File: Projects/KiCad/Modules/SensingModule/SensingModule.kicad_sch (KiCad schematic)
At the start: 40 parts, among them J1 Conn_01x02, J2 Conn_01x08, J3 Conn_01x02_Pin, J4 Micro_SD_Card_Det_Hirose_DM3AT, SW1 SW_DIP_x02, U1 MCP2562-E-P, U4 TLP222A, U5 NUCLEO-F303K8, U6 MB85RS2MT, U7 MB85RS2MT

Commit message: チップ積層セラミックコンデンサをSMD1608に変更
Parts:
- C1, C2: footprint Capacitor_SMD:C_0805_2012Metric_Pad1.18x1.45mm_HandSolder -> Capacitor_SMD:C_0603_1608Metric_Pad1.08x0.95mm_HandSolder
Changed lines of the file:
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@@
       (effects (font (size 1.27 1.27)) (justify left))
     )
-    (property "Footprint" "Capacitor_SMD:C_0805_2012Metric_Pad1.18x1.45mm_HandSolder" (at 93.6752 35.56 0)
+    (property "Footprint" "Capacitor_SMD:C_0603_1608Metric_Pad1.08x0.95mm_HandSolder" (at 93.6752 35.56 0)
       (effects (font (size 1.27 1.27)) hide)
     )
@@
       (effects (font (size 1.27 1.27)) (justify left))
     )
-    (property "Footprint" "Capacitor_SMD:C_0805_2012Metric_Pad1.18x1.45mm_HandSolder" (at 84.7852 35.56 0)
-      (effects (font (size 1.27 1.27)) hide)
-    )
+    (property "Footprint" "Capacitor_SMD:C_0603_1608Metric_Pad1.08x0.95mm_HandSolder" (at 84.7852 35.56 0)
+      (effects (font (size 1.27 1.27)) hide)
+    )

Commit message: 抵抗の在庫に合わせてサイズを変更
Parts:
- R1, R3, R4, R5, R9: footprint Resistor_SMD:R_0603_1608Metric_Pad0.98x0.95mm_HandSolder -> Resistor_SMD:R_0805_2012Metric_Pad1.20x1.40mm_HandSolder
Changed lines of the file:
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@@
       (effects (font (size 1.27 1.27)) (justify left))
     )
-    (property "Footprint" "Resistor_SMD:R_0603_1608Metric_Pad0.98x0.95mm_HandSolder" (at 230.632 48.26 90)
+    (property "Footprint" "Resistor_SMD:R_0805_2012Metric_Pad1.20x1.40mm_HandSolder" (at 230.632 48.26 90)
       (effects (font (size 1.27 1.27)) hide)
     )
@@
       (effects (font (size 1.27 1.27)) (justify left))
     )
-    (property "Footprint" "Resistor_SMD:R_0603_1608Metric_Pad0.98x0.95mm_HandSolder" (at 35.052 170.18 90)
+    (property "Footprint" "Resistor_SMD:R_0805_2012Metric_Pad1.20x1.40mm_HandSolder" (at 35.052 170.18 90)
       (effects (font (size 1.27 1.27)) hide)
     )
@@
       (effects (font (size 1.27 1.27)) (justify left))
     )
-    (property "Footprint" "Resistor_SMD:R_0603_1608Metric_Pad0.98x0.95mm_HandSolder" (at 35.052 123.19 90)
+    (property "Footprint" "Resistor_SMD:R_0805_2012Metric_Pad1.20x1.40mm_HandSolder" (at 35.052 123.19 90)
       (effects (font (size 1.27 1.27)) hide)
     )
@@
       (effects (font (size 1.27 1.27)) (justify left))
     )
-    (property "Footprint" "Resistor_SMD:R_0603_1608Metric_Pad0.98x0.95mm_HandSolder" (at 40.132 123.19 90)
+    (property "Footprint" "Resistor_SMD:R_0805_2012Metric_Pad1.20x1.40mm_HandSolder" (at 40.132 123.19 90)
       (effects (font (size 1.27 1.27)) hide)
     )
@@
       (effects (font (size 1.27 1.27)) (justify left))
     )
-    (property "Footprint" "Resistor_SMD:R_0603_1608Metric_Pad0.98x0.95mm_HandSolder" (at 220.472 48.26 90)
-      (effects (font (size 1.27 1.27)) hide)
-    )
+    (property "Footprint" "Resistor_SMD:R_0805_2012Metric_Pad1.20x1.40mm_HandSolder" (at 220.472 48.26 90)
+      (effects (font (size 1.27 1.27)) hide)
+    )

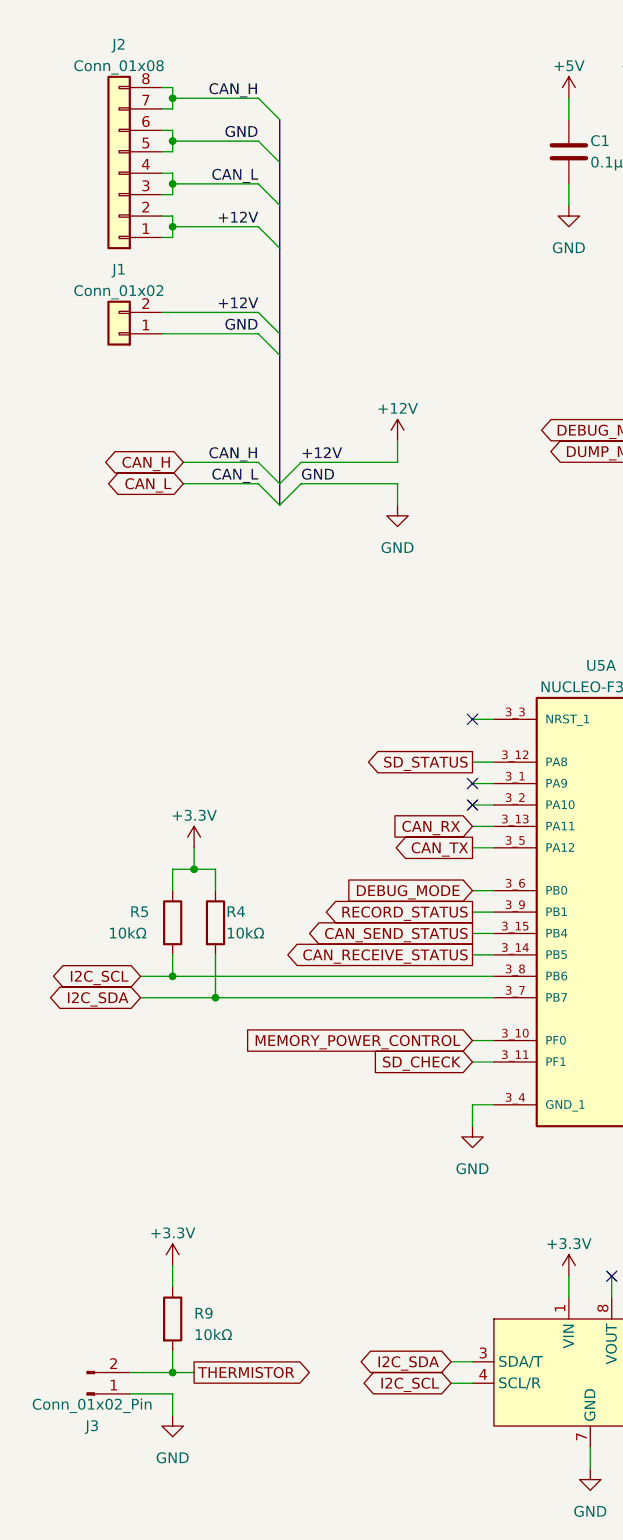
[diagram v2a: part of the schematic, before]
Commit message: コネクタ位置を揃えた
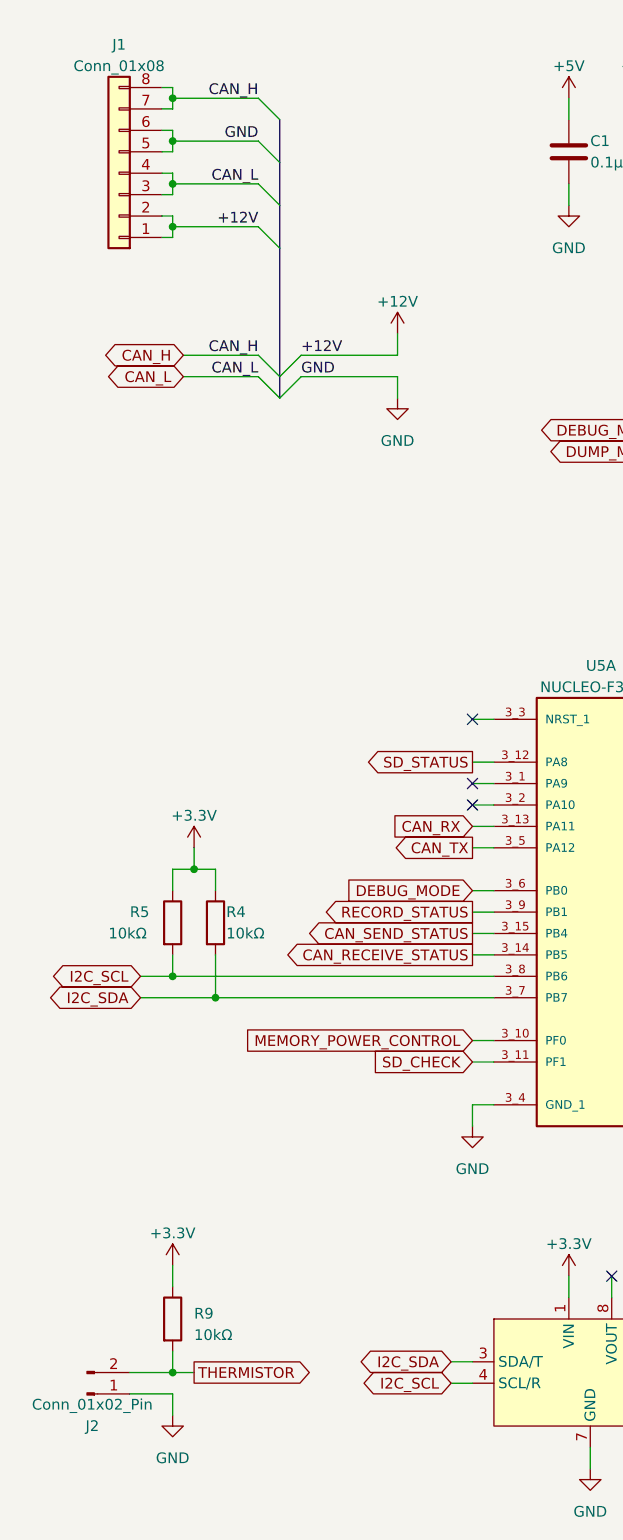
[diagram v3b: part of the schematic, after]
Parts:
- removed J1: Conn_01x02, Hirose_Connector:Hirose_DF1B, symbol Connector_Generic:Conn_01x02
- J1: renamed from J2; footprint Connector_Hirose:Hirose_DF11-8DP-2DSA_2x04_P2.00mm_Vertical -> Hirose_Connector:Hirose_DF11B-8DP-2DS
- renumbered J3 to J2
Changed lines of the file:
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@@
     (stroke (width 0) (type default))
   )
-  (bus_entry (at 49.53 71.12) (size 2.54 -2.54)
-    (stroke (width 0) (type default))
-  )
-  (bus_entry (at 46.99 53.34) (size 2.54 2.54)
-    (stroke (width 0) (type default))
-  )
-  (bus_entry (at 49.53 73.66) (size 2.54 -2.54)
+  (bus_entry (at 49.53 58.42) (size 2.54 -2.54)
+    (stroke (width 0) (type default))
+  )
+  (bus_entry (at 49.53 60.96) (size 2.54 -2.54)
     (stroke (width 0) (type default))
   )
@@
     (stroke (width 0) (type default))
   )
-  (bus_entry (at 46.99 50.8) (size 2.54 2.54)
-    (stroke (width 0) (type default))
-  )
   (bus_entry (at 46.99 30.48) (size 2.54 2.54)
     (stroke (width 0) (type default))
   )
-  (bus_entry (at 49.53 73.66) (size -2.54 -2.54)
-    (stroke (width 0) (type default))
-  )
-  (bus_entry (at 49.53 71.12) (size -2.54 -2.54)
+  (bus_entry (at 49.53 60.96) (size -2.54 -2.54)
+    (stroke (width 0) (type default))
+  )
+  (bus_entry (at 49.53 58.42) (size -2.54 -2.54)
     (stroke (width 0) (type default))
   )
@@
     (stroke (width 0) (type default))
   )
-  (wire (pts (xy 46.99 68.58) (xy 38.1 68.58))
-    (stroke (width 0) (type default))
-  )
-  (wire (pts (xy 35.56 50.8) (xy 46.99 50.8))
+  (wire (pts (xy 46.99 55.88) (xy 38.1 55.88))
     (stroke (width 0) (type default))
   )
@@
     (stroke (width 0) (type default))
   )
-  (bus (pts (xy 49.53 53.34) (xy 49.53 55.88))
-    (stroke (width 0) (type default))
-  )
   (wire (pts (xy 41.91 132.08) (xy 74.93 132.08))
     (stroke (width 0) (type default))
@@
     (stroke (width 0) (type default))
   )
-  (bus (pts (xy 49.53 71.12) (xy 49.53 73.66))
+  (bus (pts (xy 49.53 58.42) (xy 49.53 60.96))
     (stroke (width 0) (type default))
   )
@@
     (stroke (width 0) (type default))
   )
-  (wire (pts (xy 63.5 68.58) (xy 52.07 68.58))
+  (wire (pts (xy 63.5 55.88) (xy 52.07 55.88))
     (stroke (width 0) (type default))
   )
@@
     (stroke (width 0) (type default))
   )
-  (wire (pts (xy 63.5 66.04) (xy 63.5 68.58))
+  (wire (pts (xy 63.5 53.34) (xy 63.5 55.88))
     (stroke (width 0) (type default))
   )
@@
     (stroke (width 0) (type default))
   )
-  (bus (pts (xy 49.53 55.88) (xy 49.53 71.12))
+  (bus (pts (xy 49.53 43.18) (xy 49.53 58.42))
     (stroke (width 0) (type default))
   )
@@
     (stroke (width 0) (type default))
   )
-  (wire (pts (xy 46.99 71.12) (xy 38.1 71.12))
+  (wire (pts (xy 46.99 58.42) (xy 38.1 58.42))
     (stroke (width 0) (type default))
   )
@@
     (stroke (width 0) (type default))
   )
-  (bus (pts (xy 49.53 43.18) (xy 49.53 53.34))
-    (stroke (width 0) (type default))
-  )
   (wire (pts (xy 167.64 137.16) (xy 170.18 137.16))
     (stroke (width 0) (type default))
@@
     (stroke (width 0) (type default))
   )
-  (wire (pts (xy 63.5 71.12) (xy 52.07 71.12))
+  (wire (pts (xy 63.5 58.42) (xy 52.07 58.42))
     (stroke (width 0) (type default))
   )
@@
     (stroke (width 0) (type default))
   )
-  (wire (pts (xy 35.56 53.34) (xy 46.99 53.34))
-    (stroke (width 0) (type default))
-  )
   (wire (pts (xy 151.13 40.64) (xy 153.67 40.64))
     (stroke (width 0) (type default))
@@
     (stroke (width 0) (type default))
   )
-  (wire (pts (xy 63.5 73.66) (xy 63.5 71.12))
-    (stroke (width 0) (type default))
-  )
-  (label "+12V" (at 46.99 50.8 180) (fields_autoplaced)
-    (effects (font (size 1.27 1.27)) (justify right bottom))
+  (wire (pts (xy 63.5 60.96) (xy 63.5 58.42))
+    (stroke (width 0) (type default))
   )
   (label "CAN_L" (at 46.99 35.56 180) (fields_autoplaced)
@@
     (effects (font (size 1.27 1.27)) (justify right bottom))
   )
-  (label "GND" (at 46.99 53.34 180) (fields_autoplaced)
-    (effects (font (size 1.27 1.27)) (justify right bottom))
-  )
   (label "+12V" (at 46.99 40.64 180) (fields_autoplaced)
     (effects (font (size 1.27 1.27)) (justify right bottom))
   )
-  (label "GND" (at 52.07 71.12 0) (fields_autoplaced)
+  (label "GND" (at 52.07 58.42 0) (fields_autoplaced)
     (effects (font (size 1.27 1.27)) (justify left bottom))
   )
-  (label "CAN_H" (at 46.99 68.58 180) (fields_autoplaced)
+  (label "CAN_H" (at 46.99 55.88 180) (fields_autoplaced)
     (effects (font (size 1.27 1.27)) (justify right bottom))
   )
-  (label "+12V" (at 52.07 68.58 0) (fields_autoplaced)
+  (label "+12V" (at 52.07 55.88 0) (fields_autoplaced)
     (effects (font (size 1.27 1.27)) (justify left bottom))
   )
@@
     (effects (font (size 1.27 1.27)) (justify right bottom))
   )
-  (label "CAN_L" (at 46.99 71.12 180) (fields_autoplaced)
+  (label "CAN_L" (at 46.99 58.42 180) (fields_autoplaced)
     (effects (font (size 1.27 1.27)) (justify right bottom))
   )
@@
     )
   )
-  (global_label "CAN_L" (shape bidirectional) (at 38.1 71.12 180) (fields_autoplaced)
+  (global_label "CAN_L" (shape bidirectional) (at 38.1 58.42 180) (fields_autoplaced)
     (effects (font (size 1.27 1.27)) (justify right))
-    (property "Intersheetrefs" "${INTERSHEET_REFS}" (at 28.3981 71.12 0)
+    (property "Intersheetrefs" "${INTERSHEET_REFS}" (at 28.3981 58.42 0)
       (effects (font (size 1.27 1.27)) (justify right) hide)
     )
@@
     )
   )
-  (global_label "CAN_H" (shape bidirectional) (at 38.1 68.58 180) (fields_autoplaced)
+  (global_label "CAN_H" (shape bidirectional) (at 38.1 55.88 180) (fields_autoplaced)
     (effects (font (size 1.27 1.27)) (justify right))
-    (property "Intersheetrefs" "${INTERSHEET_REFS}" (at 28.0957 68.58 0)
+    (property "Intersheetrefs" "${INTERSHEET_REFS}" (at 28.0957 55.88 0)
       (effects (font (size 1.27 1.27)) (justify right) hide)
     )
@@
   (symbol (lib_id "Connector:Conn_01x02_Pin") (at 26.67 179.07 0) (mirror x) (unit 1)
     (in_bom yes) (on_board yes) (dnp no)
-    (property "Reference" "J3" (at 27.305 182.88 0)
+    (property "Reference" "J2" (at 27.305 182.88 0)
       (effects (font (size 1.27 1.27)))
     )
@@
       (project "SensingModule"
         (path "/ea1ed597-7cd3-4340-902e-bdce8f2d7a62"
-          (reference "J3") (unit 1)
+          (reference "J2") (unit 1)
         )
       )
@@
     )
   )
-  (symbol (lib_id "power:+12V") (at 63.5 66.04 0) (mirror y) (unit 1)
-    (in_bom yes) (on_board yes) (dnp no) (fields_autoplaced)
-    (property "Reference" "#PWR04" (at 63.5 69.85 0)
-      (effects (font (size 1.27 1.27)) hide)
-    )
-    (property "Value" "+12V" (at 63.5 62.23 0)
-      (effects (font (size 1.27 1.27)))
-    )
-    (property "Footprint" "" (at 63.5 66.04 0)
-      (effects (font (size 1.27 1.27)) hide)
-    )
-    (property "Datasheet" "" (at 63.5 66.04 0)
+  (symbol (lib_id "power:+12V") (at 63.5 53.34 0) (mirror y) (unit 1)
+    (in_bom yes) (on_board yes) (dnp no) (fields_autoplaced)
+    (property "Reference" "#PWR04" (at 63.5 57.15 0)
+      (effects (font (size 1.27 1.27)) hide)
+    )
+    (property "Value" "+12V" (at 63.5 49.53 0)
+      (effects (font (size 1.27 1.27)))
+    )
+    (property "Footprint" "" (at 63.5 53.34 0)
+      (effects (font (size 1.27 1.27)) hide)
+    )
+    (property "Datasheet" "" (at 63.5 53.34 0)
       (effects (font (size 1.27 1.27)) hide)
     )
@@
   (symbol (lib_id "Connector_Generic:Conn_01x08") (at 30.48 34.29 180) (unit 1)
     (in_bom yes) (on_board yes) (dnp no) (fields_autoplaced)
-    (property "Reference" "J2" (at 30.48 19.05 0)
+    (property "Reference" "J1" (at 30.48 19.05 0)
       (effects (font (size 1.27 1.27)))
     )
@@
       (effects (font (size 1.27 1.27)))
     )
-    (property "Footprint" "Connector_Hirose:Hirose_DF11-8DP-2DSA_2x04_P2.00mm_Vertical" (at 30.48 34.29 0)
+    (property "Footprint" "Hirose_Connector:Hirose_DF11B-8DP-2DS" (at 30.48 34.29 0)
       (effects (font (size 1.27 1.27)) hide)
     )
@@
       (project "SensingModule"
         (path "/ea1ed597-7cd3-4340-902e-bdce8f2d7a62"
-          (reference "J2") (unit 1)
+          (reference "J1") (unit 1)
         )
       )
@@
     )
   )
-  (symbol (lib_id "power:GND") (at 63.5 73.66 0) (mirror y) (unit 1)
-    (in_bom yes) (on_board yes) (dnp no) (fields_autoplaced)
-    (property "Reference" "#PWR05" (at 63.5 80.01 0)
-      (effects (font (size 1.27 1.27)) hide)
-    )
-    (property "Value" "GND" (at 63.5 78.74 0)
-      (effects (font (size 1.27 1.27)))
-    )
-    (property "Footprint" "" (at 63.5 73.66 0)
-      (effects (font (size 1.27 1.27)) hide)
-    )
-    (property "Datasheet" "" (at 63.5 73.66 0)
+  (symbol (lib_id "power:GND") (at 63.5 60.96 0) (mirror y) (unit 1)
+    (in_bom yes) (on_board yes) (dnp no) (fields_autoplaced)
+    (property "Reference" "#PWR05" (at 63.5 67.31 0)
+      (effects (font (size 1.27 1.27)) hide)
+    )
+    (property "Value" "GND" (at 63.5 66.04 0)
+      (effects (font (size 1.27 1.27)))
+    )
+    (property "Footprint" "" (at 63.5 60.96 0)
+      (effects (font (size 1.27 1.27)) hide)
+    )
+    (property "Datasheet" "" (at 63.5 60.96 0)
       (effects (font (size 1.27 1.27)) hide)
     )
@@
         )
       )
-    )
-  )
-  (symbol (lib_id "Connector_Generic:Conn_01x02") (at 30.48 53.34 180) (unit 1)
-    (in_bom yes) (on_board yes) (dnp no) (fields_autoplaced)
-    (property "Reference" "J1" (at 30.48 45.72 0)
-      (effects (font (size 1.27 1.27)))
-    )
-    (property "Value" "Conn_01x02" (at 30.48 48.26 0)
-      (effects (font (size 1.27 1.27)))
-    )
-    (property "Footprint" "Hirose_Connector:Hirose_DF1B" (at 30.48 53.34 0)
-      (effects (font (size 1.27 1.27)) hide)
-    )
-    (property "Datasheet" "~" (at 30.48 53.34 0)
-      (effects (font (size 1.27 1.27)) hide)
-    )
-    (pin "1")
-    (pin "2")
-    (instances
-      (project "SensingModule"
-        (path "/ea1ed597-7cd3-4340-902e-bdce8f2d7a62"
-          (reference "J1") (unit 1)
-        )
-      )

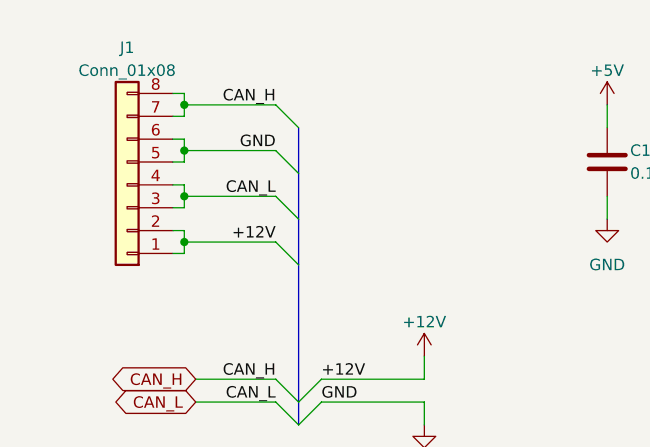
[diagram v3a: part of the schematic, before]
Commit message: コネクタのピン配置を変更
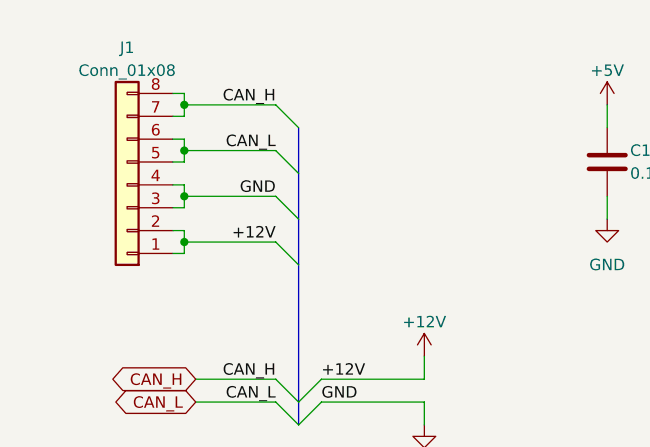
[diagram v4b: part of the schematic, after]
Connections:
- net CAN_L: now also J1.5 (Pin_5), J1.6 (Pin_6); no longer J1.3 (Pin_3), J1.4 (Pin_4)
- net GND: now also J1.3 (Pin_3), J1.4 (Pin_4); no longer J1.5 (Pin_5), J1.6 (Pin_6)
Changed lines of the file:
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@@
     (stroke (width 0) (type default))
   )
-  (label "CAN_L" (at 46.99 35.56 180) (fields_autoplaced)
+  (label "CAN_H" (at 46.99 25.4 180) (fields_autoplaced)
     (effects (font (size 1.27 1.27)) (justify right bottom))
   )
-  (label "CAN_H" (at 46.99 25.4 180) (fields_autoplaced)
+  (label "CAN_L" (at 46.99 30.48 180) (fields_autoplaced)
     (effects (font (size 1.27 1.27)) (justify right bottom))
   )
@@
     (effects (font (size 1.27 1.27)) (justify left bottom))
   )
-  (label "GND" (at 46.99 30.48 180) (fields_autoplaced)
+  (label "GND" (at 46.99 35.56 180) (fields_autoplaced)
     (effects (font (size 1.27 1.27)) (justify right bottom))
   )

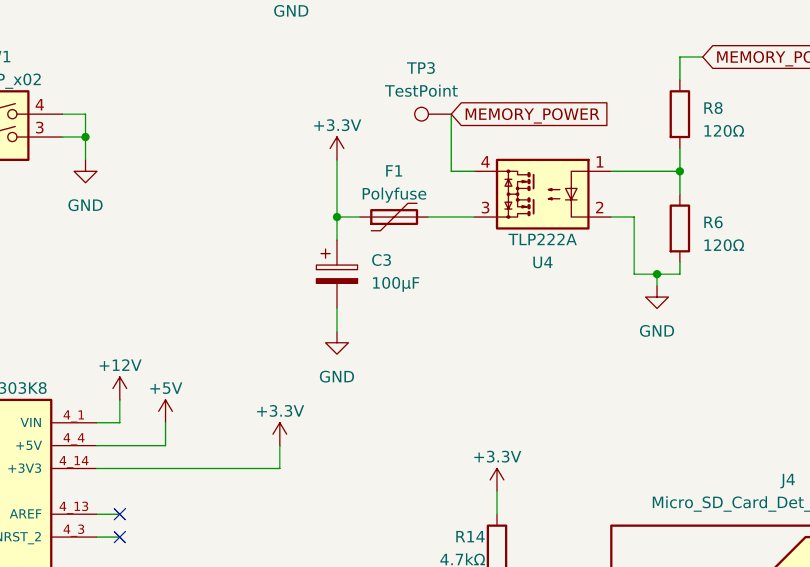
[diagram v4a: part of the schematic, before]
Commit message: バッファコンデンサを表面実装に変更
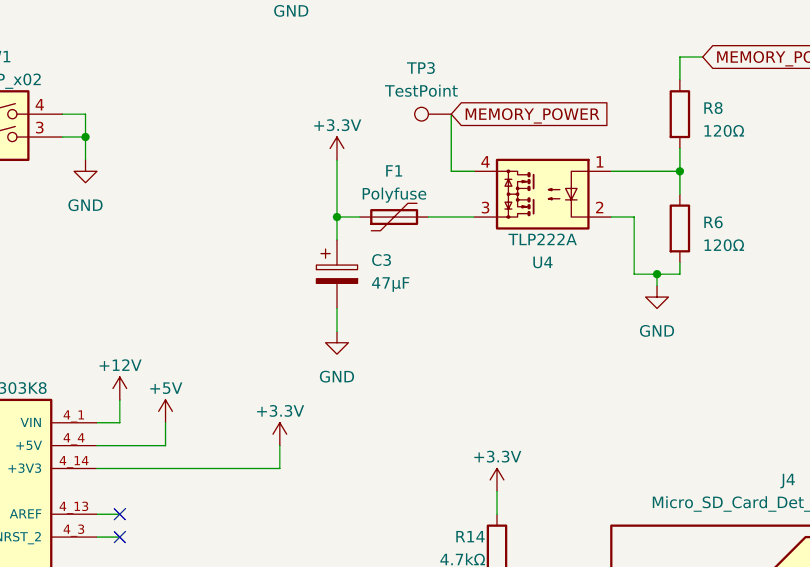
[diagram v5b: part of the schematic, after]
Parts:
- C3: value 100μF -> 47μF; footprint Capacitor_SMD:CP_Elec_6.3x7.7 -> Capacitor_SMD:CP_Elec_6.3x5.9
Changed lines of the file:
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@@
       (effects (font (size 1.27 1.27)) (justify left))
     )
-    (property "Value" "100μF" (at 147.32 83.566 0)
+    (property "Value" "47μF" (at 147.32 83.566 0)
       (effects (font (size 1.27 1.27)) (justify left))
     )
-    (property "Footprint" "Capacitor_SMD:CP_Elec_6.3x7.7" (at 144.4752 86.36 0)
+    (property "Footprint" "Capacitor_SMD:CP_Elec_6.3x5.9" (at 144.4752 86.36 0)
       (effects (font (size 1.27 1.27)) hide)
     )
